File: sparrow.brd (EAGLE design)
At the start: 80 x 80 mm, 40 parts, among them Y1 12MHz

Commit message: Further work
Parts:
- removed U$18: HEADER-2X5SMD-1.27MM, anykey:2X05_SMT
- added ADC: HEADER-1X8ROUND, anykey:1X08_ROUND
- added C22, C23: 18p, anykey:0603
- added C24, C25, C26, C30, C31, C32, C33: 100n, anykey:0603
- added C27: 1µ, anykey:0603
- added C28: 470p, anykey:0603
- added C29: 10µ, anykey:0603
- added FERRITE_BEAD: BLM18PG121SN1D, anykey:0603
- added IC1: LAN8720AQFN, anykey:QFN24-0.5-EP
- added LED2, LED3: (no value), anykey:0603_POLAR
- added P1: DEBUG, anykey:2X05_SMT
- added P2: ETHERNET_JACKPULSEJACK, anykey:PULSEJACK-J0C
- added R10, R11, R12, R13: 12K, anykey:0603
- added R14, R15: 330, anykey:0603
- added R16: 12K1, anykey:0603
- added R17, R18, R19, R20: 49R9, anykey:0603
- added X1: ABS07-32768, anykey:1206_MINIMELF_COMBO
- added Y2: (no value), anykey:CRYSTAL25X20
- moved BATT 22.0 mm to (76.0, 28.0)
- moved C10 22.0 mm to (76.0, 14.0)
- moved C11 22.0 mm to (70.0, 14.0)
- moved C8 22.0 mm to (76.0, 22.0)
- moved C9 22.0 mm to (70.0, 22.0)
- moved L1 22.0 mm to (76.0, 18.0)
- moved LED1 22.0 mm to (66.0, 17.0)
- moved PWR1 22.0 mm to (71.0, 18.0)
- moved R1 22.0 mm to (66.0, 14.0)
- moved R2 22.0 mm to (70.0, 12.0)
- moved R3 22.0 mm to (66.0, 22.0)
- moved R4 22.0 mm to (66.0, 19.0)
- moved RESET 5.37 mm to (40.4, 77.0), turned to 270 degrees
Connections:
- new net ADC0: ADC.1, MCU.6
- new net ADC1: ADC.2, MCU.2
- new net ADC2: ADC.3, MCU.143
- new net ADC3: ADC.4, MCU.139
- new net ADC4: ADC.5, MCU.138
- new net ADC5: ADC.6, MCU.144
- new net ADC6: ADC.7, MCU.142
- new net ADC7: ADC.8, MCU.136
- new net ETH_!RST: IC1.15
- new net ETH_CRS_DV: IC1.11, MCU.64
- new net ETH_MDC: IC1.13, MCU.140
- new net ETH_MDIO: IC1.12, MCU.66
- new net ETH_RBIAS: IC1.24, R16.2
- new net ETH_REFCLK: IC1.14
- new net ETH_RTERM: C33.1, R19.2, R20.1
- new net ETH_RXD0: IC1.8, MCU.62
- new net ETH_RXD1: IC1.7, MCU.32
- new net ETH_RXER: IC1.10
- new net ETH_RXN: IC1.22, P2.6, R20.2
- new net ETH_RXP: IC1.23, P2.3, R19.1
- new net ETH_TTERM: C32.1, R17.2, R18.1
- new net ETH_TXD0: IC1.17, MCU.67
- new net ETH_TXD1: IC1.18, MCU.70
- new net ETH_TXEN: IC1.16, MCU.34
- new net ETH_TXN: IC1.20, P2.2, R18.2
- new net ETH_TXP: IC1.21, P2.1, R17.1
- new net ETH_VDDCR: C27.1, C28.1, IC1.6
- new net ETH_XTAL1: IC1.5, Y2.3
- new net ETH_XTAL2: IC1.4, Y2.1
- new net N$10: IC1.2, LED3.A
- new net N$11: IC1.3, LED2.A
- new net N$3: C22.1, MCU.125, X1.2
- new net N$4: C23.1, MCU.126, X1.1
- new net N$6: LED2.K, R14.2
- new net N$7: LED3.K, R15.2
- new net SWDCLK: MCU.27, P1.4, R13.2
- new net SWDIO: MCU.30, P1.2, R10.1
- new net TDI: MCU.26, P1.8, R12.1
- new net TDO_SWO: MCU.31, P1.6, R11.1
- new net VETH33: C24.1, C25.1, C30.1, C31.1, FERRITE_BEAD.2, IC1.1, IC1.19, P2.4, P2.5
- net !RESET: now also P1.10
- net GND: now also C22.2, C23.2, C24.2, C25.2, C26.2, C27.2, C28.2, C29.2, C30.2, C31.2, C32.2, C33.2, IC1.PAD, P1.3, P1.5, P1.9, P2.8, R13.1, R14.1, R15.1, R16.1, Y2.2, Y2.4
- net VD33: now also C26.1, C29.1, FERRITE_BEAD.1, IC1.9, P1.1, R10.2, R11.2, R12.2
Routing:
- net VD33: track 299.9 -> 85.2 mm, vias 2 -> 18
- net !RESET: track 13.4 -> 56.9 mm, vias 0 -> 2
- net TDI: track 0.00 -> 28.9 mm, vias 0 -> 2
- net VETH33: track 0.00 -> 27.3 mm, vias 0 -> 4
- net SWDCLK: track 0.00 -> 25.6 mm, vias 0 -> 2
- net SWDIO: track 0.00 -> 22.0 mm, vias 0 -> 2
- net TDO_SWO: track 0.00 -> 19.7 mm, vias 0 -> 2
- net ETH_TXP: track 0.00 -> 12.2 mm
- net ETH_RXN: track 0.00 -> 11.6 mm
- net ETH_RXP: track 0.00 -> 11.5 mm, vias 0 -> 2
- net ETH_TXN: track 0.00 -> 11.3 mm, vias 0 -> 2
- net N$4: track 0.00 -> 9.31 mm
- net N$3: track 0.00 -> 5.96 mm
- net GND: track 0.00 -> 5.03 mm, vias 0 -> 2
- net ETH_TTERM: track 0.00 -> 3.42 mm
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- added copper zone on layer 16, net GND
- added copper zone on layer 2, net GND
- added copper zone on layer 1, net NC
- added copper zone on layer 15, net VD33
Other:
- outline, holes or cut-outs redrawn

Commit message: Further work
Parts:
- removed C30: 100n, anykey:0603
- removed FERRITE_BEAD: BLM18PG121SN1D, anykey:0603
- removed LED2, LED3: (no value), anykey:0603_POLAR
- removed P2: ETHERNET_JACKPULSEJACK, anykey:PULSEJACK-J0C
- added ANT1, ANT2: (no value), anykey:1206_MINIMELF_COMBO
- added C34, C52, C53, C54, R21, R29, R34: (no value), anykey:0603
- added C35, C36, C37, C56: 1µ, anykey:0603
- added C38, C39, C43, C45, C47, C49: 0.1µ, anykey:0603
- added C40, C41: 22µ, anykey:0603
- added C42, C44, C46, C48: 10µ, anykey:0603
- added C50, C51: 47µ, anykey:0805
- added C55, L5, L6: (no value), anykey:0402
- added C57, C59: 22µ 10V, anykey:0805
- added C58: 100n, anykey:0603
- added C60: 150µ 10V, anykey:1210_POLAR
- added C61: 47n, anykey:0402
- added C62, C63, C64: 100n, anykey:0402
- added C65: 1n, anykey:0402
- added C66, C67: 12p, anykey:0402
- added C68, C69: 9p, anykey:0402
- added C70, C72: 2.2p, anykey:0402
- added C71, C73: 1p, anykey:0402
- added D1, D2, D3, D4, D5: (no value), anykey:SOD123FL
- added HEADPHONE, LINEIN: (no value), anykey:1X03_ROUND
- added IC2: TLV320AIC3100VIAS, anykey:QFN23-0.5-EP-VIAS
- added IC3: TPS2500, anykey:SON10-0.5-EP
- added JP1: (no value), anykey:0603_SOLDERJUMPER_CLOSED
- added L10: 3.3nH, anykey:0402
- added L2, L3, L4: BLM18PG121SN1D, anykey:0603
- added L7: 2.2µ, anykey:INDUCTOR_40X40
- added L8: 4.7nH, anykey:0402
- added L9: 10nH, anykey:0402
- added MCU1: NRF51822QFN48, anykey:QFN48_EP
- added MIC, SPEAKER: (no value), anykey:1X02_ROUND
- added P3: HEADER-1X9ROUND, anykey:1X09_ROUND
- added P4: SD_CARD, anykey:AMPHENOL_101_00313
- added P5, P6: (no value), anykey:1X05_ROUND
- added R22, R23: 2K2, anykey:0603
- added R24, R25, R27, R28, R31, R33, R35, R36: 100K, anykey:0603
- added R26: 40K2, anykey:0603
- added R30, R32: 10K, anykey:0603
- added T1, T2, T3: (no value), anykey:SOT23
- added U$44, U$45, U$50, U$51, U$52, U$53, U$54, U$55, U$56, U$61, U$62: JUMPERSOLDER_CLOSED, anykey:0603_SOLDERJUMPER_CLOSED
- added U$6: ETHERNET_JACK_LEDSRB1-125BAG1A, anykey:RJ45-RB1-125BAG1A
- added U$68: HEADER-2X5SMD-1.27MM, anykey:2X05_SMT
- added WIFI1: CC3000EXTENDED, anykey:CC3000-EXT
- added X2: 50MHZ, anykey:CRYSTAL25X20
- added X3: 32.768KHz, anykey:1206_MINIMELF_COMBO
- L1: value 10u -> 10µH
- Y2: value (none) -> 16MHz
- moved ADC 82.2 mm to (15.0, 77.0)
- moved Y2 71.1 mm to (70.0, 11.4)
- moved R15 64.1 mm to (68.0, 49.9), turned to 270 degrees
- moved R14 62.7 mm to (66.5, 49.9), turned to 270 degrees
- moved C26 59.4 mm to (63.0, 40.6), turned to 270 degrees
- moved C29 57.7 mm to (61.4, 40.6), turned to 270 degrees
- moved C27 55.9 mm to (59.7, 40.6), turned to 270 degrees
- moved C28 54.1 mm to (58.0, 40.6), turned to 270 degrees
- moved R16 52.7 mm to (56.3, 47.6)
- moved R2 37.3 mm to (72.4, 49.2)
- moved C11 36.8 mm to (72.4, 50.7)
- moved C10 36.7 mm to (75.7, 50.7)
- moved R4 36.6 mm to (69.5, 55.4), turned to 90 degrees
- moved PWR1 36.4 mm to (72.1, 54.4)
- moved R1 36.1 mm to (69.5, 49.9), turned to 90 degrees
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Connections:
- net ETH_RXER renamed ETH_RX_ER
- removed net ETH_REFCLK: IC1.14
- removed net ETH_XTAL1: IC1.5, Y2.3
- removed net ETH_XTAL2: IC1.4, Y2.1
- removed net N$10: IC1.2, LED3.A
- removed net VBUS: USB1.1_VBUS
- removed net VEXT: MCU.21, USB0.1_VBUS
- removed net VUSB: C9.1, PWR1.2, PWR1.9, R4.2
- new net !AUDIO_PWR: T3.1
- new net !ETH_PWR: T1.1
- new net !WIFI_PWR: T2.1
- new net 5V_BOOST_SW: IC3.1, L7.P$2
- new net 5V_GEN_EN: IC3.4, R29.2
- new net 5V_ILIM: IC3.6, R26.2
- new net AUDIO_!RESET: IC2.31
- new net AUDIO_BCLK: IC2.7, U$54.2, U$55.2
- new net AUDIO_DIN: IC2.5, U$50.2
- new net AUDIO_DOUT: IC2.4, U$51.2
- new net AUDIO_GPIO1: IC2.32
- new net AUDIO_MCLK: IC2.8, U$56.2
- new net AUDIO_SCL: IC2.10, U$62.2
- new net AUDIO_SDA: IC2.9, U$61.2
- new net AUDIO_WCLK: IC2.6, U$52.2, U$53.2
- new net ETH_LED1: IC1.3, R14.2
- new net ETH_LED2: IC1.2, R15.2
- new net ETH_REF_CLK: IC1.5, MCU.45, X2.3
- new net HPL: C50.1, IC2.27
- new net HPR: C51.1, IC2.30
- new net HP_L: C50.2, HEADPHONE.1
- new net HP_R: C51.2, HEADPHONE.3
- new net I2C0_IRQA: P5.4
- new net I2C0_IRQB: P6.4
- new net I2C0_SCL: MCU.92, P5.2, P6.2, R22.1, U$62.1
- new net I2C0_SDA: MCU.93, P5.3, P6.3, R23.1, U$61.1
- new net I2S_MCLK: MCU.68, P3.3, U$56.1
- new net I2S_RX_SCK: MCU.73, P3.4, U$55.1
- new net I2S_RX_SD: MCU.78, P3.8, U$51.1
- new net I2S_RX_WS: MCU.74, P3.6, U$53.1
- new net I2S_TX_SCK: MCU.14, P3.5, U$54.1
- new net I2S_TX_SD: MCU.115, P3.9, U$50.1
- new net I2S_TX_WS: MCU.113, P3.7, U$52.1
- new net JP1: JP1.2, WIFI1.29
- new net LINEIN1: C52.1, LINEIN.3
- new net LINEIN2: C53.1, LINEIN.1
- new net MIC: C54.1, IC2.11, MIC.2, R21.1
- new net MIC1LM: C52.2, IC2.15
- new net MIC1LP: C53.2, IC2.13
- new net MIC1RP: C54.2, IC2.14
- new net MICBIAS: IC2.12, R21.2
- new net N$12: U$45.1, WIFI1.28
- new net N$13: C67.P$1, MCU1.38, Y2.1
- new net N$14: C66.P$1, MCU1.37, Y2.3
- new net N$15: C62.P$1, MCU1.39
- new net N$16: C61.P$1, MCU1.29
- new net N$17: C69.P$2, MCU1.46, X3.1
- new net N$18: C68.P$2, MCU1.45, X3.2
- new net N$19: R14.1, U$6.L1
- new net N$20: D5.A, U$44.2
- new net N$21: L8.P$1, L9.P$2, MCU1.31
- new net N$22: R15.1, U$6.L4
- new net N$23: C70.P$1, L8.P$2, MCU1.32
- new net N$24: C70.P$2, C71.P$2, L10.P$1
- new net N$25: ANT2.1, C73.P$2, L10.P$2
- new net N$27: C72.P$2, L9.P$1, MCU1.30
- new net N$5: C55.P$1, L5.P$2, WIFI1.35
- new net NRF_SWDCLK: MCU1.24, R34.2, U$68.4
- new net NRF_SWDIO: MCU1.23, U$68.2
- new net SD_CD: MCU.60, P4.CD, R24.1
- new net SD_CLK: MCU.99, P4.5
- new net SD_CMD: MCU.49, P4.2
- new net SD_DAT0: MCU.52, P4.7
- new net SD_DAT1: MCU.53, P4.8
- new net SD_DAT2: MCU.55, P4.9
- new net SD_DAT3: MCU.56, P4.1
- new net SD_WP: P4.WP, R25.1
- new net SPKM: IC2.19, IC2.23, SPEAKER.2
- new net SPKP: IC2.22, IC2.26, SPEAKER.1
- new net USB0_VBUS: MCU.21, R30.1, R31.2
- new net USB1_VBUS: MCU.91, R32.1, R33.2
- new net USB_PPWR: IC3.7, MCU.75, R28.2
- new net USB_PWR_FAULT: IC3.8, MCU.81, R27.1
- new net V5_GEN: C59.1, D3.A, IC3.10
- new net V5_IN: C9.1, D1.K, D2.K, PWR1.2, PWR1.9, R35.2, R4.2
- new net V5_IN_SENSE: R35.1, R36.2
- new net V5_OUT: D3.K, D4.K, D5.K
- new net VAUDIO33: C37.1, C42.1, C43.1, C44.1, C45.1, C46.1, C47.1, C48.1, C49.1, IC2.17, IC2.2, IC2.28, IC2.3, L4.2
- new net VAUDIO5: C38.1, C39.1, C40.1, C41.1, IC2.21, IC2.24
- new net VETH_RAW: L2.1, T1.3
- new net VETH_RAW1: L3.1, T2.3
- new net VETH_RAW2: L4.1, T3.3
- new net VPOWER: D1.A, D4.A
- new net VUSB0: C60.A, IC3.9, R30.2, USB0.1_VBUS
- new net VUSB1: D2.A, R32.2, U$44.1, USB1.1_VBUS
- new net VWIFI33: C36.1, L3.2, WIFI1.19, WIFI1.23
- new net WIFI_CLK: WIFI1.17
- new net WIFI_IRQ: WIFI1.14
- new net WIFI_MISO: WIFI1.13
- new net WIFI_MOSI: WIFI1.15
- new net WIFI_SSEL: WIFI1.12
- new net WIFI_SW_EN: WIFI1.26
- net ETH_RXN: now also U$6.R8; no longer P2.6
- net ETH_RXP: now also U$6.R7; no longer P2.3
- net ETH_TXN: now also U$6.R2; no longer P2.2
- net ETH_TXP: now also U$6.R1; no longer P2.1
- net GND: now also C34.2, C35.2, C36.2, C37.2, C38.2, C39.2, C40.2, C41.2, C42.2, C43.2, C44.2, C45.2, C46.2, C47.2, C48.2, C49.2, C56.2, C57.2, C58.2, C59.2, C60.K, C61.P$2, C62.P$2, C63.P$2, C64.P$2, C65.P$2, C66.P$2, C67.P$2, C68.P$1, C69.P$1, C71.P$1, C72.P$1, C73.P$1, HEADPHONE.2, IC2.1, IC2.16, IC2.18, IC2.20, IC2.25, IC2.29, IC2.PAD, IC2.VIA1, IC2.VIA2, IC2.VIA3, IC2.VIA4, IC2.VIA5, IC2.VIA6, IC2.VIA7, IC2.VIA8, IC2.VIA9, IC3.2, IC3.5, IC3.PAD, IC3.THERM1, IC3.THERM2, IC3.THERM3, IC3.THERM4, IC3.THERM5, L5.P$1, L6.P$1, LINEIN.2, MIC.1, P3.1, P4.3, P4.6, P4.GND1, P4.GND2, P5.5, P6.5, R26.1, R28.1, R29.1, R31.1, R33.1, R34.1, R36.1, U$6.CHASSIS@1, U$6.CHASSIS@2, U$6.L2, U$68.3, U$68.5, U$68.7, U$68.9, WIFI1.1, WIFI1.10, WIFI1.11, WIFI1.16, WIFI1.18, WIFI1.20, WIFI1.21, WIFI1.22, WIFI1.25, WIFI1.31, WIFI1.32, WIFI1.33, WIFI1.34, WIFI1.36, WIFI1.37, WIFI1.38, WIFI1.39, WIFI1.40, WIFI1.41, WIFI1.42, WIFI1.43, WIFI1.44, WIFI1.45, WIFI1.46, WIFI1.9, X2.2; no longer C30.2, P2.8, R14.1, R15.1
- net N$11: now also JP1.1, WIFI1.30; no longer IC1.3, LED2.A
- net N$6: now also ANT1.1, C55.P$2, L6.P$2; no longer LED2.K, R14.2
- net N$7: now also U$45.2, WIFI1.27; no longer LED3.K, R15.2
- net VBAT: now also C57.1, C58.1, IC3.3, L7.P$1
- net VD33: now also C56.1, C63.P$1, C64.P$1, C65.P$1, MCU1.1, MCU1.12, MCU1.35, MCU1.36, P3.2, P4.4, P5.1, P6.1, R22.2, R23.2, R24.2, R25.2, R27.2, T1.2, T2.2, T3.2, U$68.1; no longer C26.1, C29.1, FERRITE_BEAD.1, IC1.9
- net VETH33: now also C26.1, C29.1, C34.1, C35.1, IC1.9, L2.2, U$6.L3, U$6.R3, X2.1, X2.4; no longer C30.1, FERRITE_BEAD.2, P2.4, P2.5
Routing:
- net VETH33: track 27.3 -> 96.0 mm, vias 4 -> 5
- net I2C0_SCL: track 0.00 -> 61.3 mm, vias 0 -> 2
- net V5_IN: track 0.00 -> 58.1 mm, vias 0 -> 4
- net I2C0_SDA: track 0.00 -> 57.4 mm, vias 0 -> 2
- net VUSB0: track 0.00 -> 54.4 mm, vias 0 -> 2
- net VAUDIO33: track 0.00 -> 42.3 mm, vias 0 -> 4
- net ETH_RXD1: track 0.00 -> 39.2 mm, vias 0 -> 2
- net SD_CLK: track 0.00 -> 38.4 mm, vias 0 -> 2
- net ETH_TXEN: track 0.00 -> 38.4 mm, vias 0 -> 2
- net N$19: track 0.00 -> 37.7 mm, vias 0 -> 1
- net VEXT: track 33.8 -> 0.00 mm, vias 2 -> 0
- net USB1_VBUS: track 0.00 -> 30.3 mm, vias 0 -> 2
- net GND: track 5.03 -> 34.8 mm, vias 2 -> 80
- net ETH_REF_CLK: track 0.00 -> 28.8 mm, vias 0 -> 2
- net USB0_VBUS: track 0.00 -> 28.5 mm, vias 0 -> 2
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- removed copper zone on layer 1, net NC
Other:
- board size 80 x 80 mm -> 100 x 100 mm

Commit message: Further work
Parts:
- removed L2, L3, L4: BLM18PG121SN1D, anykey:0603
- removed P6: (no value), anykey:1X05_ROUND
- removed T1, T2, T3: (no value), anykey:SOT23
- added !PGM: PUSHBUTTONKMR2XX, anykey:CK-KMR2
- added C30, C74, C75: 0.1µ, anykey:0603
- added C76, C77, C78, C79, C80: 1µ, anykey:0603
- added I2C0, I2C1, P2: (no value), anykey:1X05_ROUND
- added IC4, IC5, IC6, IC7, IC8: SKYWORKS_AAT4280ASC70JW-8-NOTHERMALS, anykey:SC70JW-8-NOTHERMALS
- added IC9: FXMA10820-DFN, anykey:FXMA108
- added J1: (no value), anykey:CUI_PJ_102BH
- added JP2, JP3, SPI0: HEADER-1X7ROUND, anykey:1X07_ROUND
- added R37: 100K, anykey:0603
- added R38, R39: 2K2, anykey:0603
- added U$19: JUMPERSOLDER_CLOSED, anykey:0603_SOLDERJUMPER_CLOSED
- added U$26: HEADER-2X5SMD-1.27MM, anykey:2X05_SMT
- C24, C25, C26, C31, C32, C33, C58, C62, C63, C64: value 100n -> 0.1µ
- C34: value (none) -> 0.1µ
- C35, C36, C37: value 1µ -> 0.1µ
- C61: value 47n -> 0.047µ
- C65: value 1n -> 1000p
- IC1: value LAN8720AQFN -> LAN8720AVIAS; device anykey:QFN24-0.5-EP -> anykey:QFN24-0.5-EP-VIAS
- P3: value HEADER-1X9ROUND -> HEADER-1X10ROUND; device anykey:1X09_ROUND -> anykey:1X10_ROUND
- P5: device anykey:1X05_ROUND -> anykey:1X06_ROUND
- moved P5 88.4 mm to (6.00, -16.0)
- moved D4 65.4 mm to (22.5, 74.1)
- moved D1 62.8 mm to (22.5, 76.5)
- moved R22 61.6 mm to (55.1, 32.0), turned to 0 degrees
- moved R23 57.2 mm to (51.7, 32.0)
- moved C36 20.6 mm to (15.4, 6.50), turned to 180 degrees
- moved D3 20.6 mm to (70.2, 74.3), turned to 90 degrees
- moved U$50 20.3 mm to (57.8, 35.7)
- moved ADC 20.2 mm to (1.91, 61.6), turned to 90 degrees
- moved R10 16.3 mm to (25.4, 34.0), turned to 180 degrees
- moved JP1 16.3 mm to (20.2, 16.3)
- moved U$51 15.2 mm to (60.3, 35.7)
- moved R13 14.7 mm to (25.4, 35.2), turned to 0 degrees
- moved C35 14.5 mm to (66.7, 40.7), turned to 0 degrees
- moved C37 13.2 mm to (59.0, 25.9), turned to 180 degrees
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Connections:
- net I2S_MCLK renamed I2S_RX_MCLK
- net N$1 renamed USB0_RREF
- net N$13 renamed BT_XC2
- net N$14 renamed BT_XC1
- net N$15 renamed BT_DEC1
- net N$16 renamed BT_DEC2
- net N$17 renamed BT_XL1
- net N$18 renamed BT_XL2
- net N$2 renamed CHARGE_SW
- net N$21 renamed BT_ANT1
- net N$23 renamed BT_ANT2
- net N$24 renamed BT_ANT_UNBAL
- net N$25 renamed BT_ANT
- net N$27 renamed BT_VDD_PA
- net N$3 renamed RTXC1
- net N$4 renamed RTXC2
- net N$5 renamed WIFI_ANT_UNBAL
- net N$6 renamed WIFI_ANT
- net N$8 renamed CHARGE_!CHRG
- net USB_PPWR renamed USB0_PPWR
- net USB_PWR_FAULT renamed USB0_PWR_FAULT
- removed net !AUDIO_PWR: T3.1
- removed net !ETH_PWR: T1.1
- removed net !WIFI_PWR: T2.1
- removed net I2C0_IRQA: P5.4
- removed net I2C0_IRQB: P6.4
- removed net JP1: JP1.2, WIFI1.29
- removed net N$11: JP1.1, WIFI1.30
- removed net N$12: U$45.1, WIFI1.28
- removed net N$7: U$45.2, WIFI1.27
- removed net VETH_RAW: L2.1, T1.3
- removed net VETH_RAW1: L3.1, T2.3
- removed net VETH_RAW2: L4.1, T3.3
- removed net WIFI_CLK: WIFI1.17
- removed net WIFI_MISO: WIFI1.13
- removed net WIFI_MOSI: WIFI1.15
- removed net WIFI_SSEL: WIFI1.12
- new net !PGM: !PGM.P$3, !PGM.P$4, MCU.96, R37.1
- new net AUDIO_PWR: IC6.3, IC7.3
- new net ETH_PWR: IC4.3
- new net GPIO5V_1: IC9.16, JP2.3
- new net GPIO5V_2: IC9.15, JP2.4
- new net GPIO5V_3: IC9.14, JP2.5
- new net GPIO5V_4: IC9.13, JP2.6
- new net GPIO5V_5: IC9.12, JP2.7
- new net GPIO_1: IC9.5
- new net GPIO_2: IC9.6
- new net GPIO_3: IC9.7
- new net GPIO_4: IC9.8
- new net GPIO_5: IC9.9
- new net I2C0_IRQ: I2C0.5
- new net I2C1_IRQ: I2C1.5
- new net I2C1_SCL: I2C1.3, MCU.88, R39.1
- new net I2C1_SDA: I2C1.4, MCU.87, R38.1
- new net I2S_TX_MCLK: MCU.112, P3.10
- new net PORT_PWR_5V: IC8.3
- new net SPI0_IRQ: SPI0.6
- new net SPI0_MISO: MCU.122, SPI0.2
- new net SPI0_MOSI: MCU.123, SPI0.3
- new net SPI0_SCK: MCU.118, SPI0.5
- new net SPI0_SSEL: MCU.124, SPI0.4
- new net SPI1_MISO: MCU.44, WIFI1.13
- new net SPI1_MOSI: MCU.47, WIFI1.15
- new net SPI1_SCK: MCU.120, WIFI1.17
- new net SPI1_SSEL: MCU.48, WIFI1.12
- new net UART0_RXD: IC9.3, MCU.82
- new net UART0_RXD_5V: IC9.18, P2.4
- new net UART0_TXD: IC9.2, MCU.80
- new net UART0_TXD_5V: IC9.19, P2.3
- new net UART0_UCLK: IC9.4, MCU.84
- new net UART0_UCLK_5V: IC9.17, P2.5
- new net UART1_CTS: MCU.57
- new net UART1_DCD: MCU.58
- new net UART1_DSR: MCU.37
- new net UART1_DTR: MCU.39
- new net UART1_RI: MCU.54
- new net UART1_RTS: MCU.46
- new net UART1_RXD: MCU.65
- new net UART1_TXD: MCU.63
- new net UART2_DIR: MCU.108, P5.6
- new net UART2_RXD: MCU.105, P5.4
- new net UART2_TXD: MCU.104, P5.3
- new net UART2_UCLK: MCU.106, P5.5
- new net UART3_BAUD: JP3.7, MCU.7
- new net UART3_DIR: JP3.6, MCU.9
- new net UART3_RXD: JP3.4, MCU.8
- new net UART3_TXD: JP3.3, MCU.3
- new net UART3_UCLK: JP3.5, MCU.1
- new net VPORT5: C75.1, IC8.2, IC9.20, JP2.1, P2.1
- new net WIFI_PWR: IC5.3
- new net WIFI_SCL_CC3000: JP1.1, U$26.8, WIFI1.30
- new net WIFI_SCL_EEPROM: JP1.2, U$26.9, WIFI1.29
- new net WIFI_SDA_CC3000: U$26.6, U$45.1, WIFI1.28
- new net WIFI_SDA_EEPROM: U$26.7, U$45.2, WIFI1.27
- new net WL_EN1: U$19.1, U$26.2, WIFI1.7
- new net WL_EN2: U$19.2, U$26.3, WIFI1.5
- new net WL_RS232_RX: U$26.5, WIFI1.8
- new net WL_RS232_TX: U$26.4, WIFI1.6
- net GND: now also !PGM.P$1, !PGM.P$2, C30.2, C74.2, C75.2, C76.2, C77.2, C78.2, C79.2, C80.2, I2C0.2, I2C1.2, IC1.P$1, IC1.P$2, IC1.P$3, IC1.P$4, IC4.4, IC5.4, IC6.4, IC7.4, IC8.4, IC9.10, IC9.11, J1.1, J1.2, JP2.2, JP3.2, MCU.102, MCU.42, P2.2, P3.2, P5.2, SPI0.7, U$26.10; no longer P3.1, P5.5, P6.5
- net I2C0_SCL: now also I2C0.3; no longer P5.2, P6.2
- net I2C0_SDA: now also I2C0.4; no longer P5.3, P6.3
- net V5_OUT: now also C79.1, C80.1, IC7.1, IC7.5, IC7.6, IC7.7, IC7.8, IC8.1, IC8.5, IC8.6, IC8.7, IC8.8
- net VAUDIO33: now also IC6.2; no longer L4.2
- net VAUDIO5: now also C74.1, IC7.2
- net VD33: now also C76.1, C77.1, C78.1, I2C0.1, I2C1.1, IC4.1, IC4.5, IC4.6, IC4.7, IC4.8, IC5.1, IC5.5, IC5.6, IC5.7, IC5.8, IC6.1, IC6.5, IC6.6, IC6.7, IC6.8, IC9.1, JP3.1, MCU.29, MCU.43, MCU.98, P3.1, R37.2, R38.2, R39.2, SPI0.1; no longer P3.2, P6.1, T1.2, T2.2, T3.2
- net VETH33: now also IC4.2; no longer L2.2
- net VPOWER: now also J1.3
- net VWIFI33: now also C30.1, IC5.2, U$26.1; no longer L3.2
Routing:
- net V5_OUT: track 0.00 -> 215.3 mm, vias 1 -> 5
- net SPI1_SCK: track 0.00 -> 68.1 mm, vias 0 -> 2
- net USB0_PWR_FAULT: track 0.00 -> 63.2 mm, vias 0 -> 2
- net USB0_PPWR: track 2.22 -> 61.7 mm, vias 0 -> 2
- net I2C1_SDA: track 0.00 -> 54.7 mm, vias 0 -> 1
- net I2S_TX_SCK: track 0.00 -> 54.7 mm, vias 0 -> 1
- net I2C1_SCL: track 0.00 -> 52.7 mm, vias 0 -> 1
- net ETH_MDC: track 1.12 -> 51.4 mm, vias 1 -> 2
- net SPI0_SCK: track 0.00 -> 48.0 mm, vias 0 -> 1
- net UART0_TXD: track 0.00 -> 47.9 mm, vias 0 -> 2
- net I2C0_SDA: track 57.4 -> 104.4 mm, vias 2 -> 3
- net UART0_RXD: track 0.00 -> 46.9 mm, vias 0 -> 2
- net UART0_UCLK: track 0.00 -> 46.4 mm, vias 0 -> 2
- net SPI1_MOSI: track 0.00 -> 45.6 mm, vias 0 -> 2
- net I2S_TX_WS: track 0.00 -> 44.3 mm, vias 0 -> 1
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
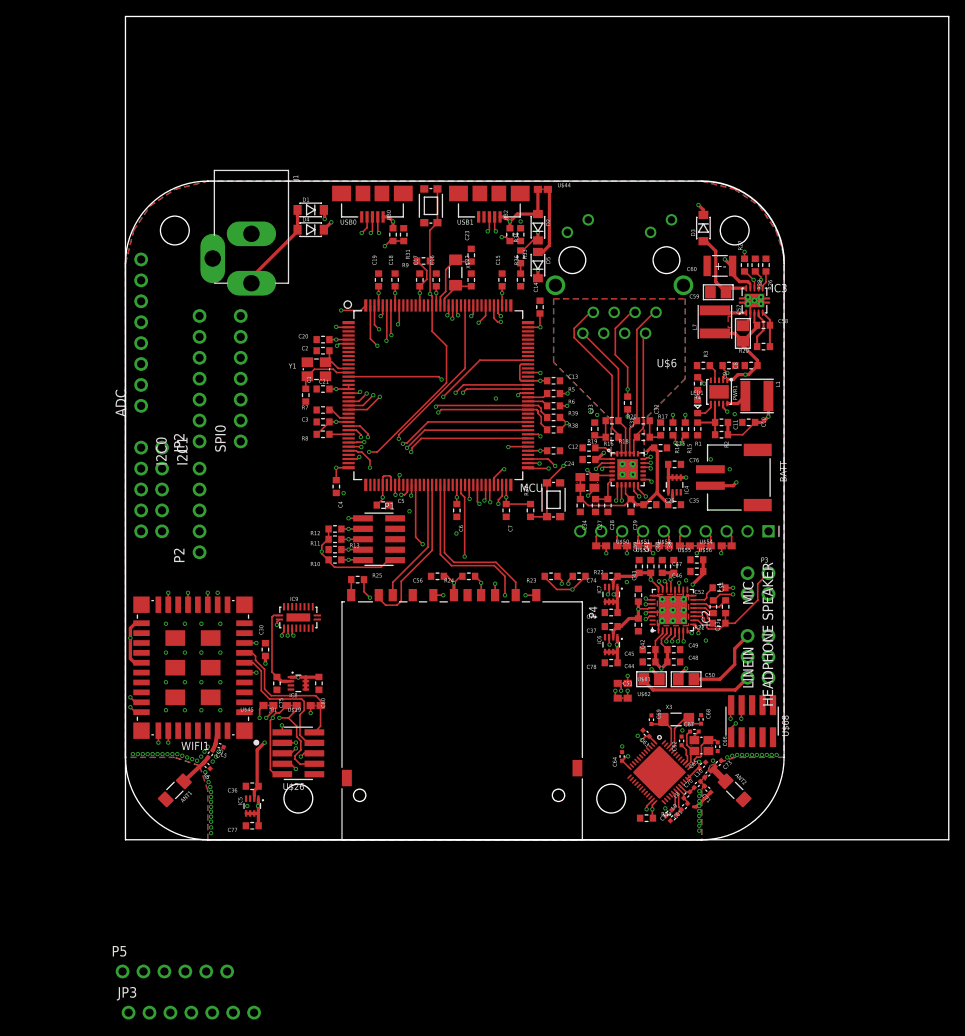
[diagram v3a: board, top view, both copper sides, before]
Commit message: positioned and connected headers
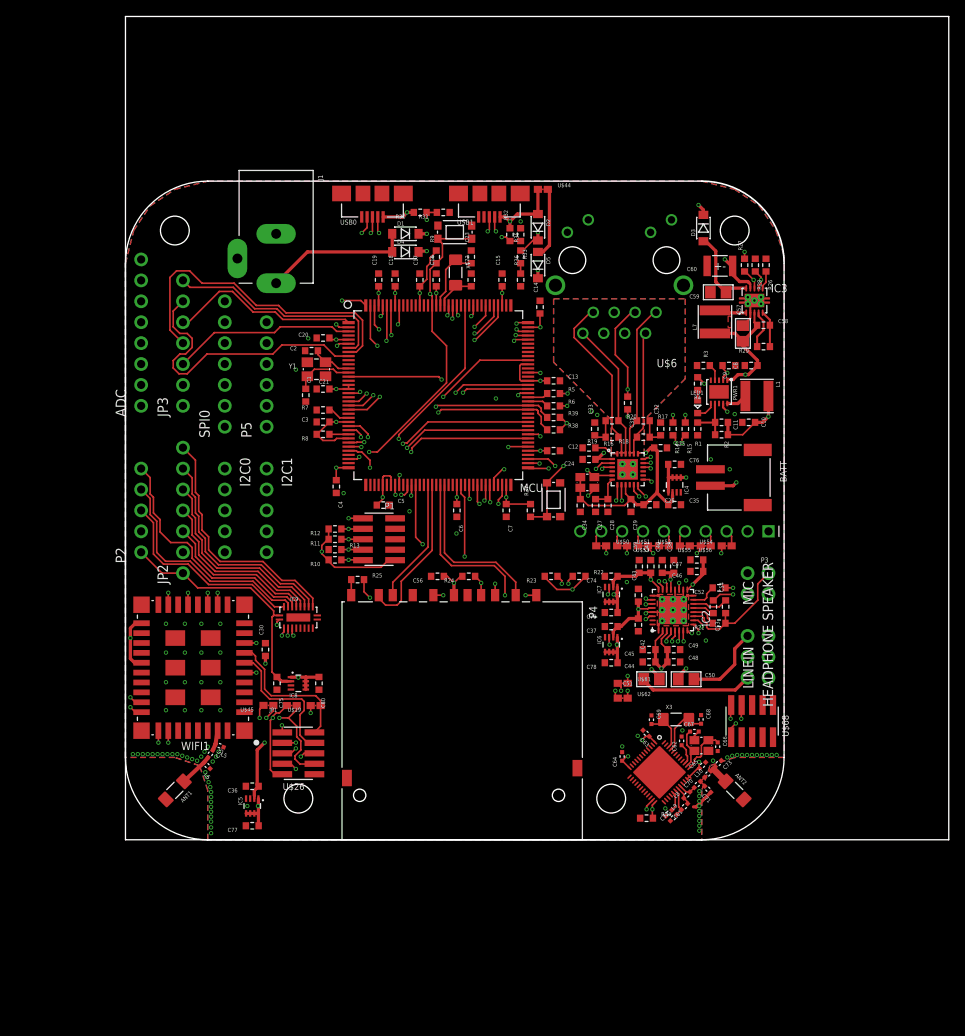
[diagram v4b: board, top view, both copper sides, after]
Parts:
- IC2: device anykey:QFN23-0.5-EP-VIAS -> anykey:QFN32-0.5-EP-VIAS
- moved JP3 81.3 mm to (6.99, 60.3), turned to 90 degrees
- moved P5 73.4 mm to (17.1, 56.5), turned to 90 degrees
- moved JP2 16.1 mm to (6.99, 40.0)
- moved I2C1 13.0 mm to (17.1, 40.0)
- moved D1 11.9 mm to (34.0, 73.6)
- moved D4 11.8 mm to (34.0, 71.4)
- moved I2C0 10.5 mm to (12.1, 40.0)
- moved P2 7.10 mm to (1.91, 40.0)
- moved R31 5.51 mm to (38.6, 76.2), turned to 180 degrees
- moved RESET 4.32 mm to (40.0, 73.8), turned to 270 degrees
- moved R30 4.26 mm to (35.8, 76.2), turned to 180 degrees
- moved J1 3.00 mm to (18.3, 70.6)
- moved SPI0 2.63 mm to (12.1, 57.8)
- moved R9 1.63 mm to (37.8, 70.8), turned to 90 degrees
- moved C2 1.40 mm to (22.6, 59.4)
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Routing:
- net UART3_RXD: track 0.00 -> 40.0 mm
- net UART2_DIR: track 0.00 -> 39.0 mm, vias 0 -> 1
- net UART2_TXD: track 0.00 -> 38.8 mm, vias 0 -> 1
- net UART2_UCLK: track 0.00 -> 37.7 mm, vias 0 -> 1
- net UART2_RXD: track 0.00 -> 36.9 mm, vias 0 -> 1
- net UART3_DIR: track 0.00 -> 35.0 mm
- net GPIO5V_5: track 0.00 -> 29.8 mm
- net UART0_UCLK_5V: track 0.00 -> 29.5 mm
- net UART3_BAUD: track 0.00 -> 27.6 mm
- net UART0_RXD_5V: track 0.00 -> 27.4 mm
- net GPIO5V_4: track 0.00 -> 27.1 mm
- net UART0_TXD_5V: track 0.00 -> 24.4 mm
- net GPIO5V_3: track 0.00 -> 24.3 mm
- net UART3_UCLK: track 0.00 -> 23.2 mm
- net ADC0: track 33.8 -> 56.2 mm
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
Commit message: layout refinements
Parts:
- moved C32 8.39 mm to (66.2, 58.2), turned to 0 degrees
- moved C33 8.39 mm to (55.8, 58.2), turned to 180 degrees
- moved C29 7.50 mm to (64.1, 47.6)
- moved R17 7.31 mm to (63.2, 58.2)
- moved R18 7.31 mm to (63.2, 56.2)
- moved R19 7.31 mm to (58.8, 56.2)
- moved R20 7.31 mm to (58.8, 58.2)
- moved C26 7.27 mm to (61.4, 47.6), turned to 270 degrees
- moved C25 7.22 mm to (64.5, 54.8)
- moved C24 7.00 mm to (56.3, 53.2)
- moved C27 7.00 mm to (57.1, 47.6)
- moved C28 7.00 mm to (58.6, 47.6)
- moved C34 7.00 mm to (55.2, 47.6)
- moved IC1 7.00 mm to (61.0, 52.0)
- moved R16 7.00 mm to (56.3, 54.6)
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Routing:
- net VETH33: track 98.7 -> 87.8 mm
- net ETH_RXD1: track 39.7 -> 46.8 mm
- net ETH_TXN: track 15.2 -> 8.23 mm
- net ETH_TXP: track 18.9 -> 11.9 mm
- net ETH_RXN: track 16.8 -> 10.4 mm
- net ETH_MDC: track 57.1 -> 51.1 mm
- net ETH_RXP: track 20.7 -> 14.9 mm
- net TDI: track 35.4 -> 30.1 mm
- net !RESET: track 52.0 -> 46.9 mm
- net N$22: track 26.8 -> 22.2 mm
- net N$19: track 37.7 -> 33.1 mm
- net ETH_TXEN: track 40.3 -> 43.6 mm
- net ETH_TXD1: track 28.0 -> 30.9 mm
- net ETH_TXD0: track 27.3 -> 30.1 mm
- net ETH_MDIO: track 25.5 -> 28.4 mm
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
